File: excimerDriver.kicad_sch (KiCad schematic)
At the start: 58 parts, among them IC3 STM32G071KBT6, IC4 INA210, J1 B04B-XASK-1_LF__SN_, J2 B08B-XASK-1-A_LF__SN_, J3 TC2030, J4 BM02B-SRSS-TB_LF__SN_, J5 B4B-PH-K-S_LF__SN_, Q2 DCX114EU-7-F, Q3 BC817-40

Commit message: Final Rev. 1.0.0
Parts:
- R28, R30: value 100R 0603 -> 10R 0603
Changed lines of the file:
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@@
 			)
 		)
-		(property "Value" "100R 0603"
+		(property "Value" "10R 0603"
 			(at 43.942 147.574 90)
 			(effects
@@
 			)
 		)
-		(property "Value" "100R 0603"
+		(property "Value" "10R 0603"
 			(at 43.7442 150.114 90)
 			(effects

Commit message: Final Version Rev. 2.0.0
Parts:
- added TPB1, TPB2: UV LED, TestPoint:TestPoint_Pad_D1.0mm, symbol Connector:TestPoint
- C1: value 1u X7R 50V 0805 -> 1u X7R 0805
- C101: renamed from C2; value 100µ 35V -> 330µ 35V
- C16, C17, C5: value 10µ X7R 50V 1210 -> 10µ X7R 1210
- F1: value 2A -> 1A
- L2: value L -> 10uH
- renumbered Q2 to T2, Q3 to T3
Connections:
- net +3V3: now also TPB1.1
- net at IC3.12 (PA5): now also TPB2.1
- net at R42.1, T3.3 (C): no longer TP5.1
- net at R39.2, T3.1 (B): now also TP5.1
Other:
- moved on the sheet: TP5

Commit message: Fixed BoM, and added jobset.
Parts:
- C1: LCSC Part Number (none) -> C28323; Manufacturer_Part_Number (none) -> CL21B105KBFNNNE
- C101: LCSC Part Number (none) -> C88770; Manufacturer_Part_Number (none) -> 35ZLJ330M8X20
- C16, C17, C5: LCSC Part Number (none) -> C138687; Manufacturer_Part_Number (none) -> CL32B106KBJNNNE
- C24, C6: LCSC Part Number (none) -> C2915770; Manufacturer_Part_Number (none) -> SCC2211X222K502TS
- C25, C27, C28, C29, C3, C4: LCSC Part Number (none) -> C15725; Manufacturer_Part_Number (none) -> CL10B104KC8NNNC
- C26: LCSC Part Number (none) -> C153291; Manufacturer_Part_Number (none) -> CL10B102KC8NNNC
- D10: LCSC Part Number (none) -> C1983631; Manufacturer_Part_Number (none) -> 3KASMC24A
- D11: LCSC Part Number (none) -> C965799; Manufacturer_Part_Number (none) -> XL-1608SURC-06
- D12: LCSC Part Number (none) -> C965804; Manufacturer_Part_Number (none) -> XL-1608UGC-04
- D13, D14: LCSC Part Number (none) -> C531179
- F1: LCSC Part Number (none) -> C2934573; Manufacturer_Part_Number (none) -> 0440001.WR
- F2: LCSC Part Number (none) -> C185112; Manufacturer_Part_Number (none) -> MF-NSMF020-2
- IC3: LCSC Part Number (none) -> C529348
- IC4: LCSC Part Number (none) -> C353893; Manufacturer_Part_Number (none) -> INA210AIDCKR
- J1: LCSC Part Number (none) -> C264994
- J2: LCSC Part Number (none) -> C491710
- J4: LCSC Part Number (none) -> C160388
- J5: LCSC Part Number (none) -> C131334
- L1: Manufacturer_Part_Number (none) -> 744045008
- L2: LCSC Part Number (none) -> C88182; Manufacturer_Part_Number (none) -> MLZ2012N100LT000
- R27, R36, R38, R39: LCSC Part Number (none) -> C22548; Manufacturer_Part_Number (none) -> RC0603FR-071KL
- R28, R30: LCSC Part Number (none) -> C109318; Manufacturer_Part_Number (none) -> RC0603FR-0710RL
- R29, R44, R45: LCSC Part Number (none) -> C105588; Manufacturer_Part_Number (none) -> RC0603FR-07100RL
- R31, R32: LCSC Part Number (none) -> C114668; Manufacturer_Part_Number (none) -> RC0603FR-071K5L
- R33, R34, R37: LCSC Part Number (none) -> C98220; Manufacturer_Part_Number (none) -> RC0603FR-0710KL
- R35: LCSC Part Number (none) -> C728292; Manufacturer_Part_Number (none) -> PA1206FRF470R02L
- R40, R41: LCSC Part Number (none) -> C125931; Manufacturer_Part_Number (none) -> AC0603FR-072K2L
- R42, R43: LCSC Part Number (none) -> C114549; Manufacturer_Part_Number (none) -> RC0805FR-07680RL
- T2: LCSC Part Number (none) -> C460018
- T3: LCSC Part Number (none) -> C52801; Manufacturer_Part_Number (none) -> BC817-40,215
- TP1, TP2, TP3, TP4, TP5, TP6, TP7, TPB1, TPB2: now left out of the parts list

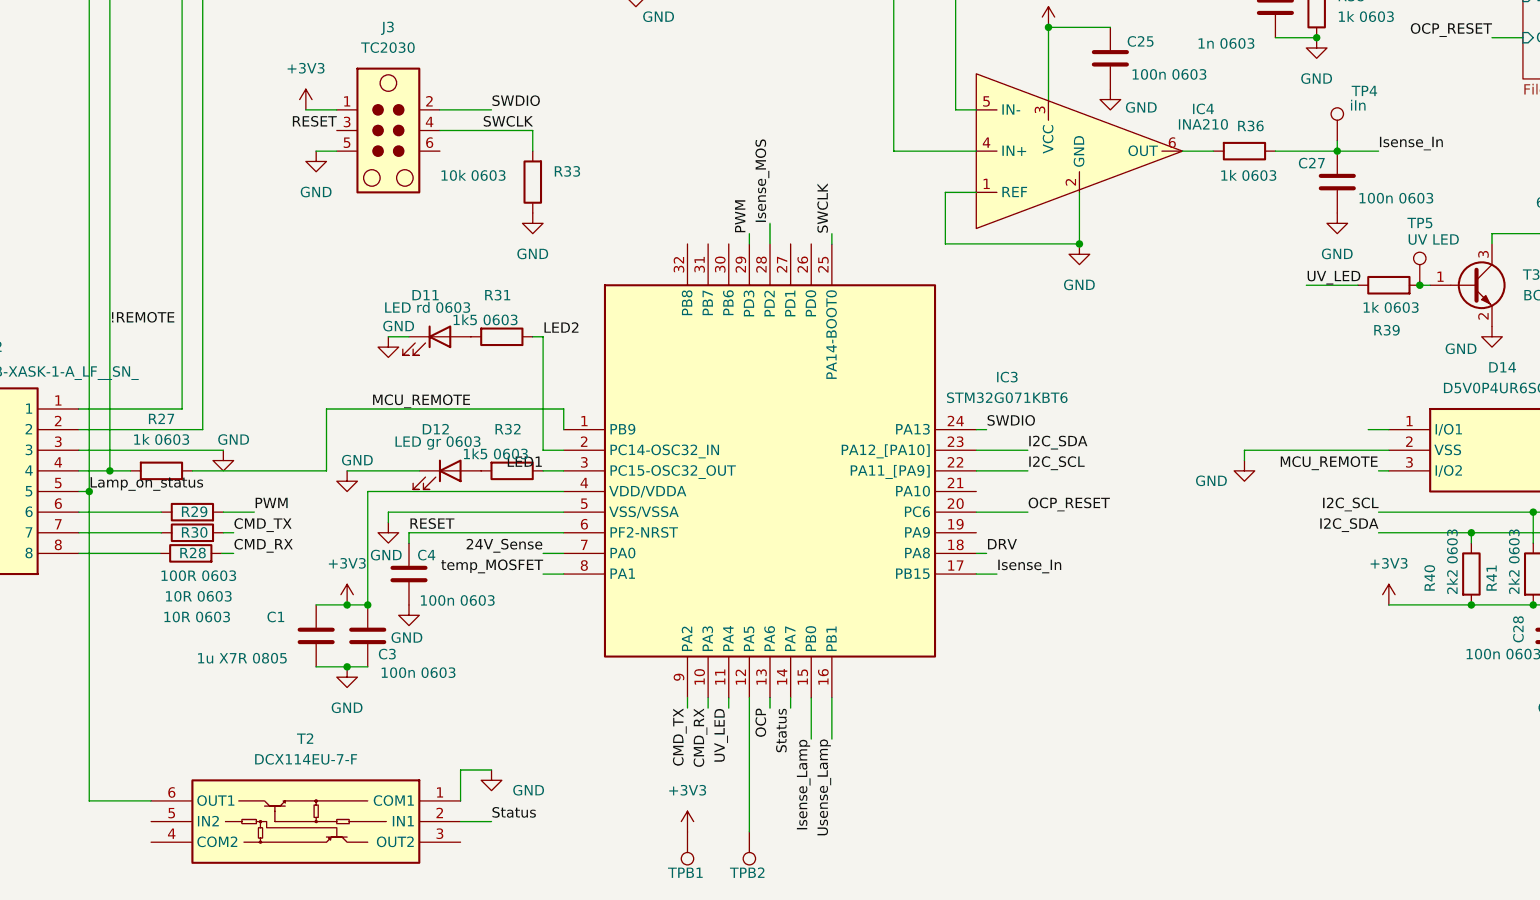
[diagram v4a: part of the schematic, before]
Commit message: Fixed debug header footprint, and cleaned up silkscreen.
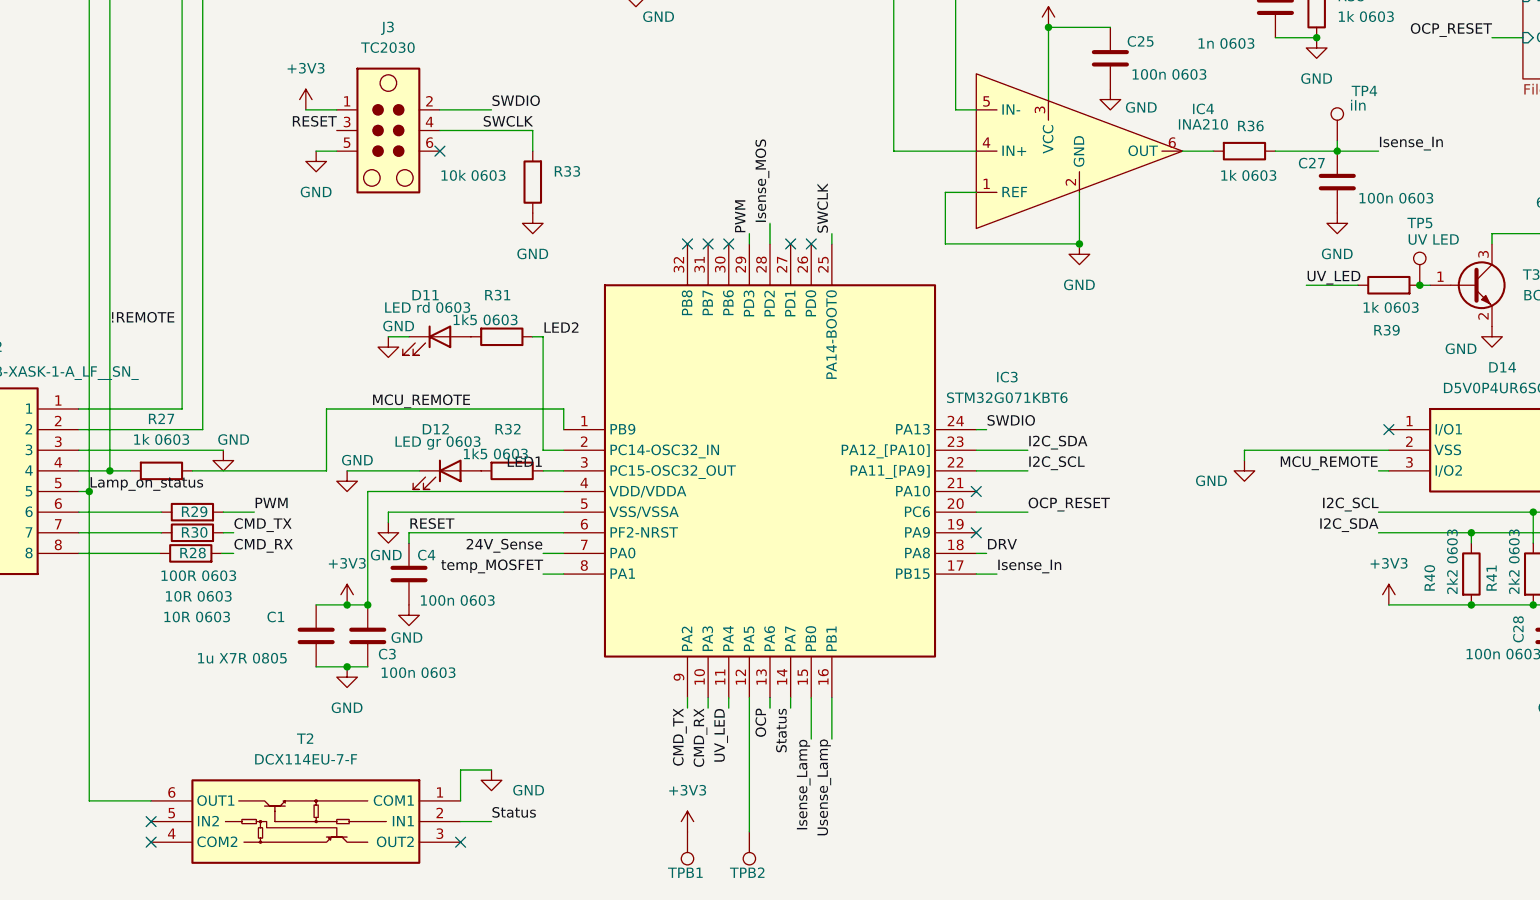
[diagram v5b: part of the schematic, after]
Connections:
- no-connect marks 0 -> 12
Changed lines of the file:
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@@
 		(color 0 0 0 0)
 	)
+	(no_connect
+		(at 119.38 104.14)
+	)
+	(no_connect
+		(at 106.68 104.14)
+	)
+	(no_connect
+		(at 38.1 175.26)
+	)
+	(no_connect
+		(at 139.7 139.7)
+	)
+	(no_connect
+		(at 73.66 92.71)
+	)
+	(no_connect
+		(at 104.14 104.14)
+	)
+	(no_connect
+		(at 139.7 134.62)
+	)
+	(no_connect
+		(at 38.1 177.8)
+	)
+	(no_connect
+		(at 116.84 104.14)
+	)
+	(no_connect
+		(at 109.22 104.14)
+	)
+	(no_connect
+		(at 76.2 177.8)
+	)
+	(no_connect
+		(at 190.5 127)
+	)
 	(wire
 		(pts
@@
 		)
 		(stroke
-			(width 0)
-			(type default)
-		)
-	)
-	(wire
-		(pts
-			(xy 187.96 127) (xy 190.5 127)
-		)
-		(stroke

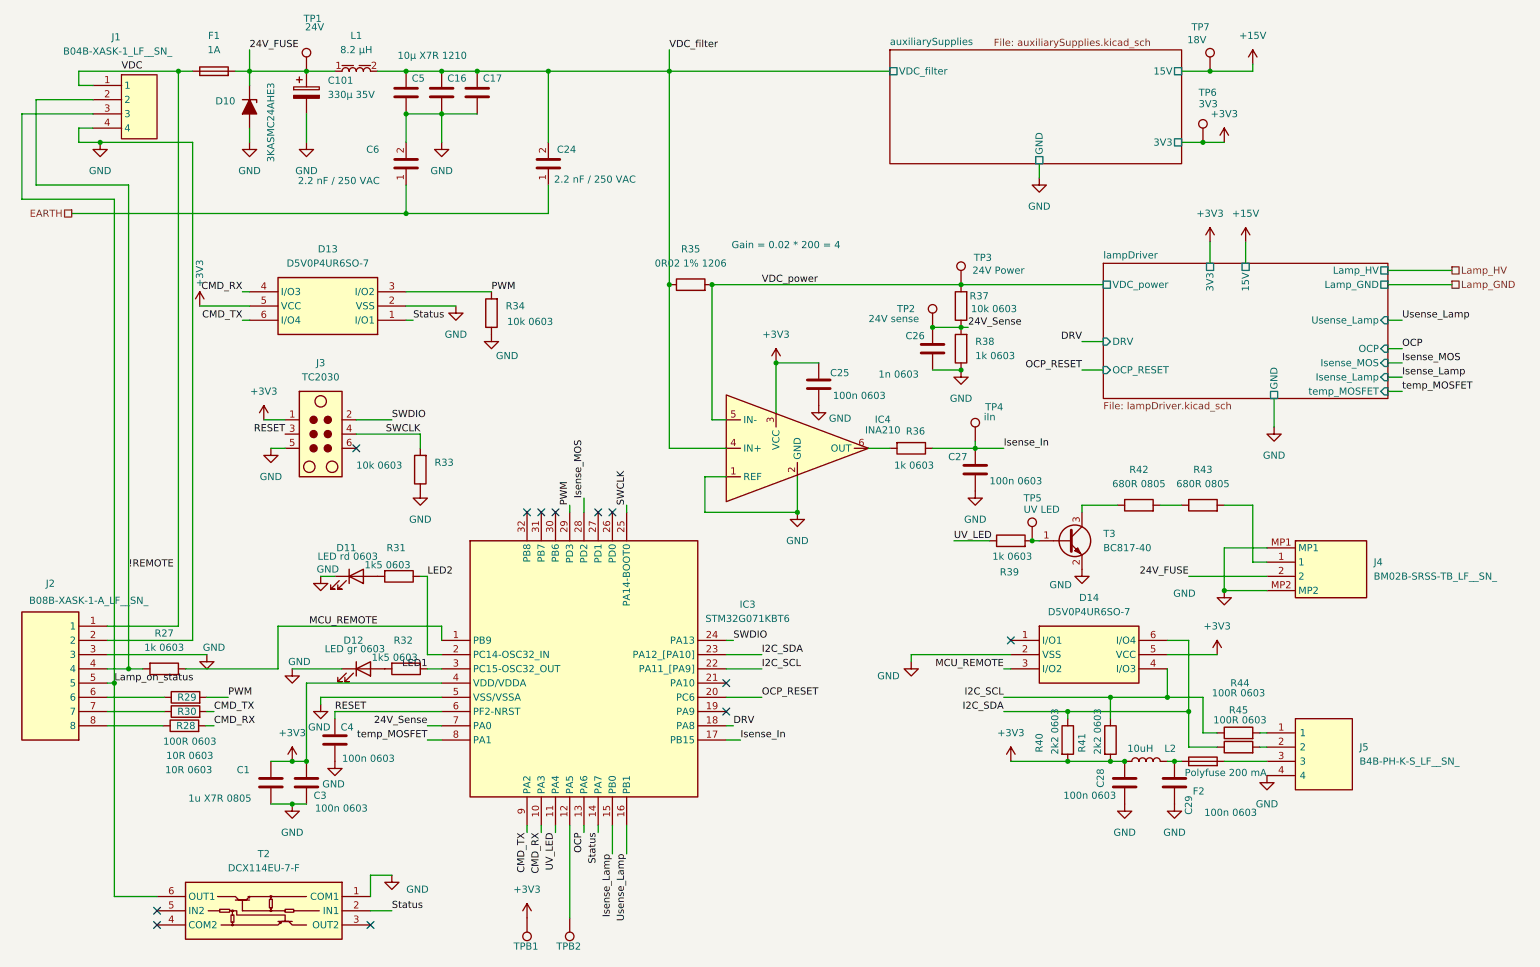
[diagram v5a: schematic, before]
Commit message: Fixed transformer footprint, and cleaned up silkscreen.
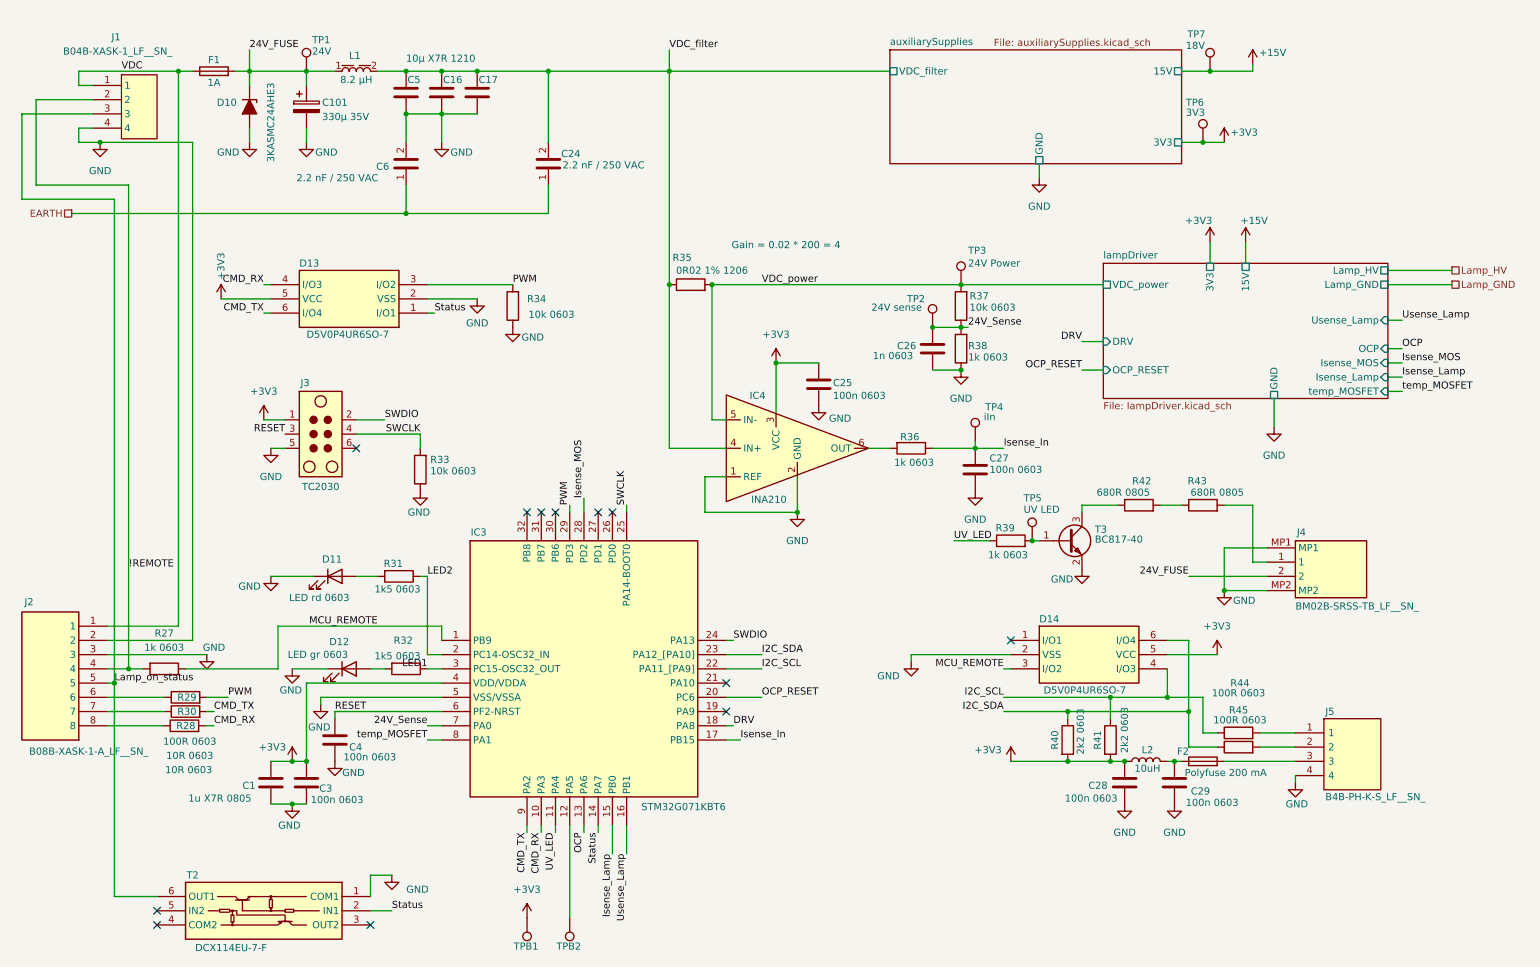
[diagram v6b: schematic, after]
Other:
- moved on the sheet: C101, D11, D12, D13, J5, R34
